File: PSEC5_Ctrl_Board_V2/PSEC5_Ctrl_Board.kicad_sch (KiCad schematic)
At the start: 12 parts

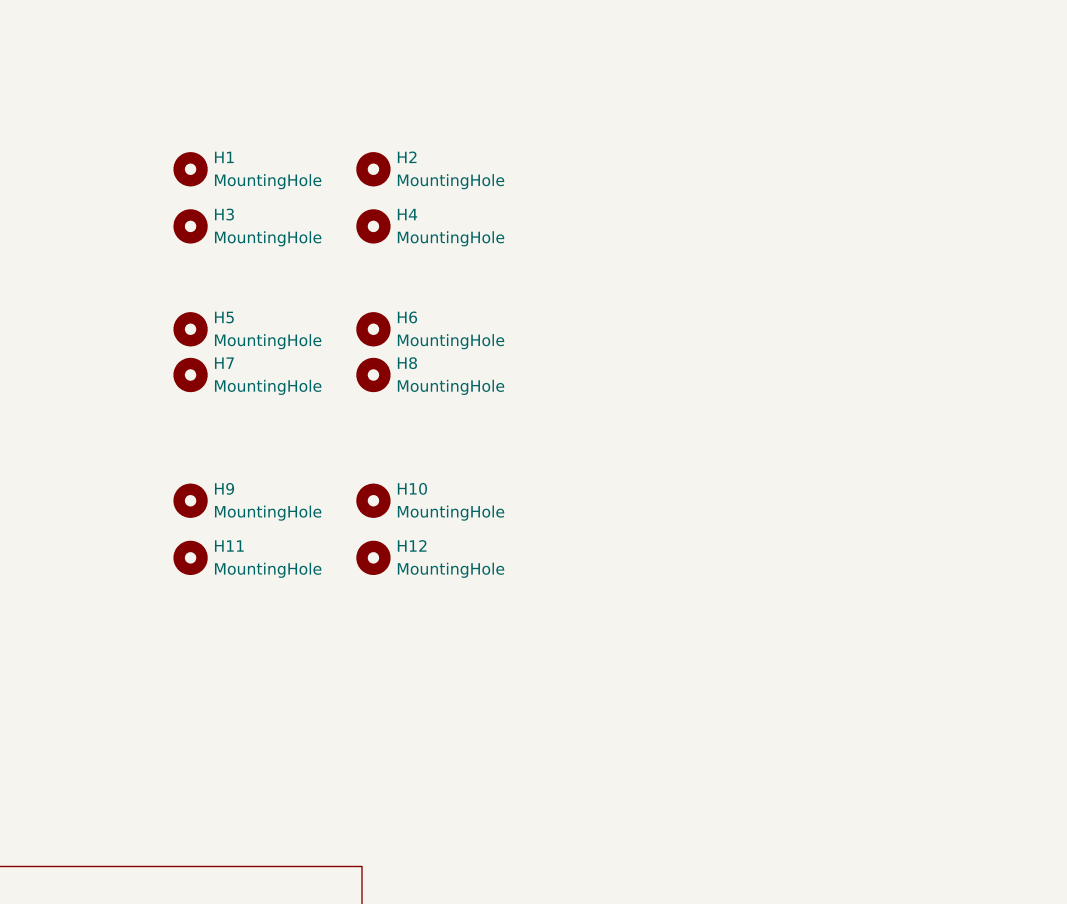
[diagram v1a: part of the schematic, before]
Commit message: added spacer footprints
Final change will be silkscreen, board is ready to be looked at
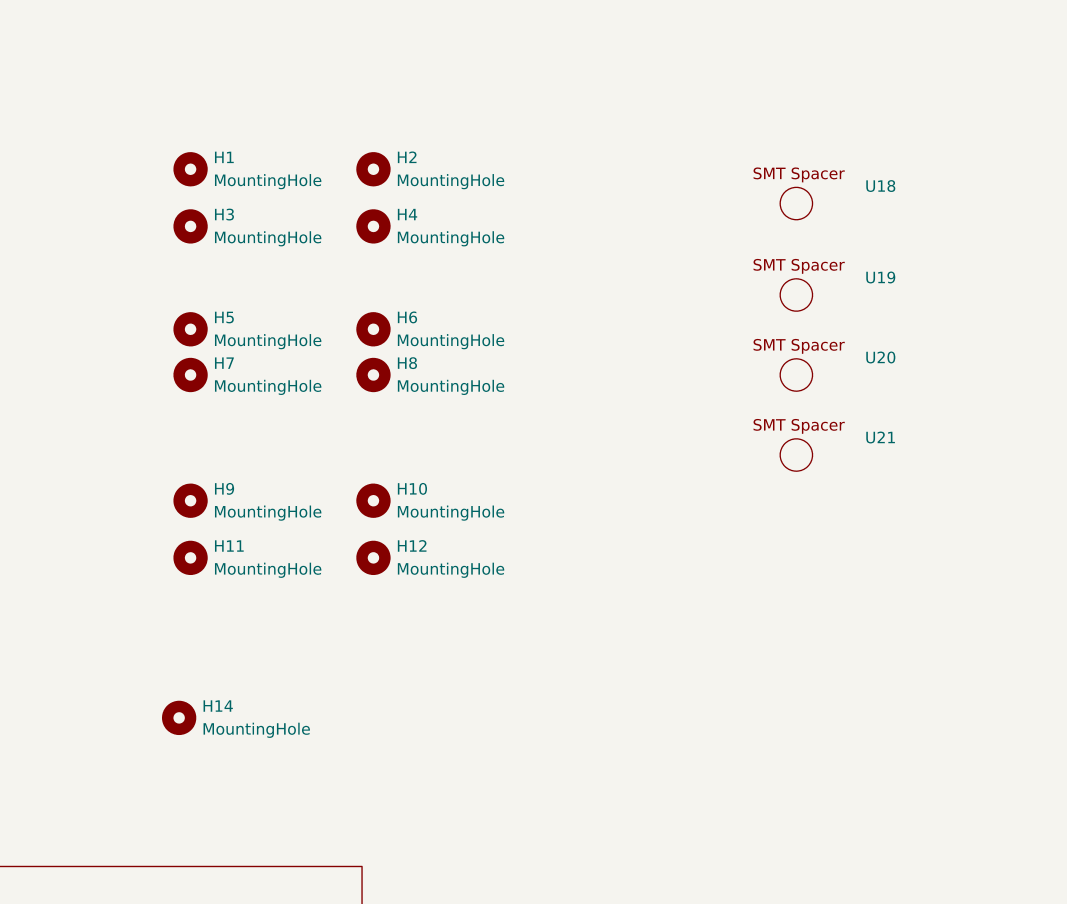
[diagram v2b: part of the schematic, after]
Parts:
- added H14: MountingHole, MountingHole:MountingHole_2.2mm_M2_DIN965, symbol Mechanical:MountingHole
- added U18, U19, U20, U21: ~, 9774050360R:9774050360R, symbol 9774050360R:9774050360R
